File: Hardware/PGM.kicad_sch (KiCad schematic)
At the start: 6 parts, among them Q4 2N7002K, U2 HS1602A-B

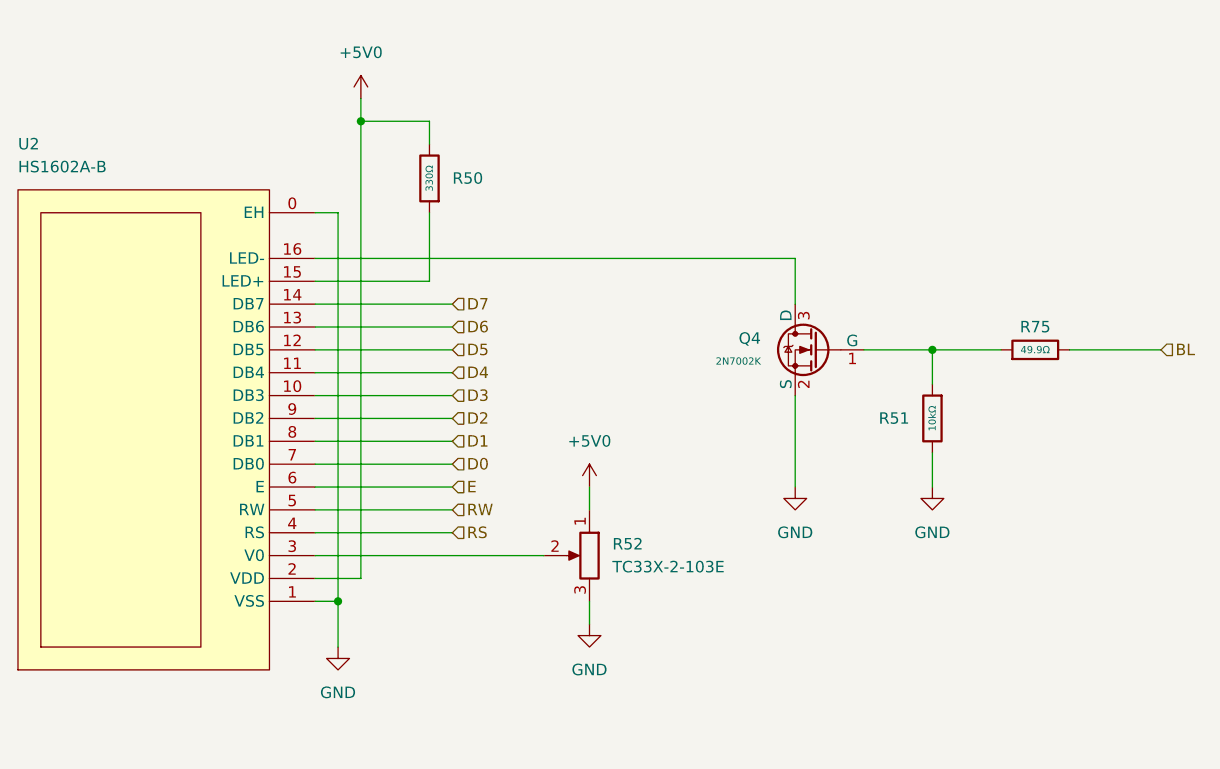
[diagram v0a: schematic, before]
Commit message: remove unused sheets
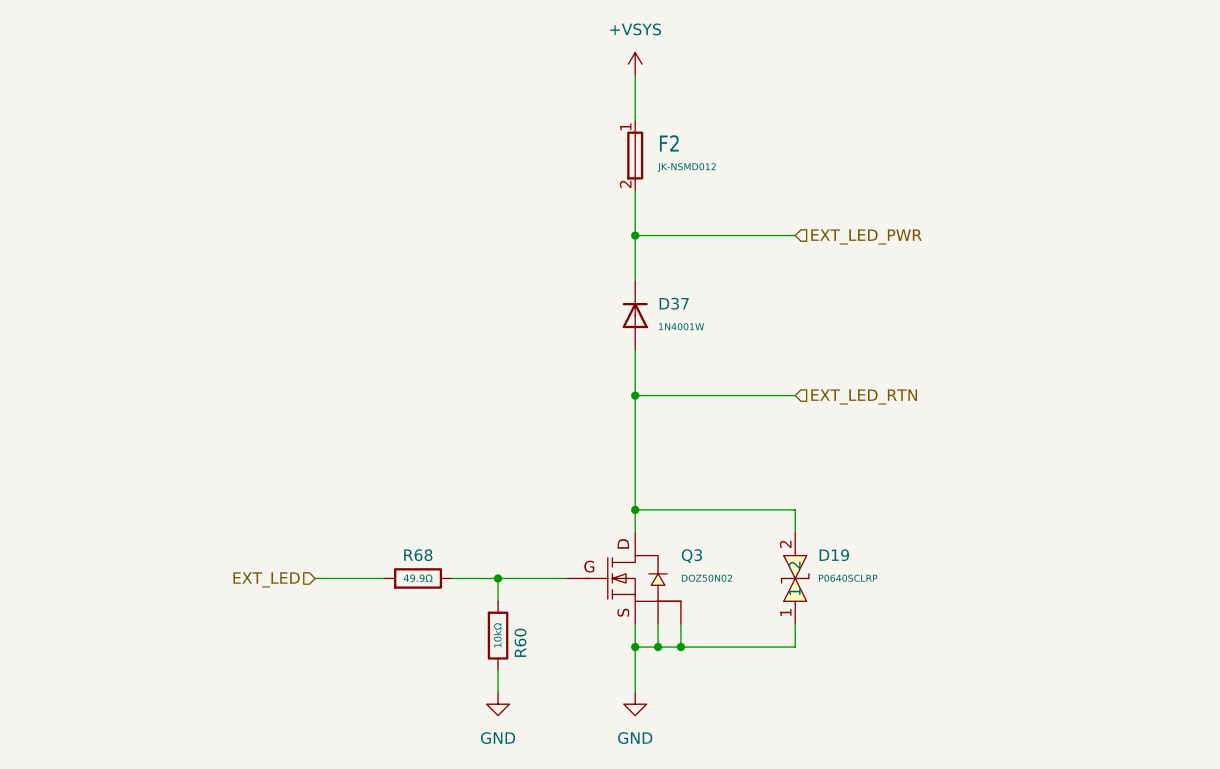
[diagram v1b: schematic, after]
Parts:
- removed Q4: 2N7002K, PCM_JLCPCB:Q_SOT-23, symbol PCM_JLCPCB-Transistors:NMOS,2N7002K
- removed R50: 330Ω, PCM_JLCPCB:R_0603, symbol PCM_JLCPCB-Resistors:0603,330Ω
- removed R51: 10kΩ, PCM_JLCPCB:R_0603, symbol PCM_JLCPCB-Resistors:0603,10kΩ
- removed R52: TC33X-2-103E, EasyEDA:RES-ADJ-SMD_3P-L3.0-W3.8-P1.75-BR, symbol AderbTech:POT, TC33X-2-103E
- removed R75: 49.9Ω, PCM_JLCPCB:R_0603, symbol PCM_JLCPCB-Resistors:0603,49.9Ω
- removed U2: HS1602A-B, EasyEDA:LCD1602, symbol EasyEDA:HS1602A-B
- added D19: P0640SCLRP, EasyEDA:SMB_L4.6-W3.6-LS5.3-BI, symbol EasyEDA:P0640SCLRP
- added D37: 1N4001W, PCM_JLCPCB:D_SOD-123FL, symbol PCM_JLCPCB-Diodes:General,1N4001W
- added F2: JK-NSMD012, EASYEDA2KICAD:F1206, symbol EASYEDA2KICAD:Fuse, JK-NSMD012
- added Q3: DOZ50N02, EasyEDA:PDFN3333-8_L3.1-W3.2-P0.65-LS3.4-BL_1, symbol EasyEDA:DOZ50N02
- added R60: 10kΩ, PCM_JLCPCB:R_0603, symbol PCM_JLCPCB-Resistors:0603,10kΩ
- added R68: 49.9Ω, PCM_JLCPCB:R_0603, symbol PCM_JLCPCB-Resistors:0603,49.9Ω
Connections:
- net GND: now also D19.1, Q3.1 (S), Q3.2 (S), Q3.3 (S), R60.2
- new net: Q3.4 (G), R60.1, R68.2
- new net +VSYS: F2.1
- new net EXT_LED: R68.1
- new net EXT_LED_PWR: D37.1, F2.2
- new net EXT_LED_RTN: D19.2, D37.2, Q3.5 (D)
